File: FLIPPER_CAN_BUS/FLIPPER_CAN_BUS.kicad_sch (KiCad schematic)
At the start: 24 parts, among them J1 Conn_01x02, J1 Conn_01x08_Socket, J2 Conn_01x10_Socket, U1 TJA1051T/3, U2 MCP2515-xST, U3 AP3602AKTR-G1, Y1 16 Mhz

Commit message: Change_Capacitor_BOM
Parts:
- C1, C5: manf# C0603C470J4GACAUTO -> FN18N220J500PSG
- C10, C12, C13, C8: LCSC# (none) -> C326057; Proveedor Mouser -> LCSC; manf# KAM15CT70J106KT -> CC0603KRX5R6BB106
- C11, C2, C7, C9: LCSC# (none) -> C282519; Proveedor Mouser -> LCSC; manf# 0603F104Z160CT -> TCC0603X7R104K500CT
- C3, C4: LCSC# (none) -> C525244; Proveedor Mouser -> LCSC
- C6: LCSC# (none) -> C26413; Proveedor Mouser -> LCSC; manf# 06035C105KAT2A -> CL10A105KP8NNNC
- R1, R3: LCSC# (none) -> C99198; Proveedor Mouser -> LCSC; manf# RP0603DRD0710KL -> RC0603JR-0710KL
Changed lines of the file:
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@@
       (effects (font (size 1.27 1.27)) hide)
     )
-    (property "manf#" "KAM15CT70J106KT" (at 208.153 106.172 0)
-      (effects (font (size 1.27 1.27)) hide)
-    )
-    (property "Proveedor" "Mouser" (at 208.153 106.172 0)
+    (property "manf#" "CC0603KRX5R6BB106" (at 208.153 106.172 0)
+      (effects (font (size 1.27 1.27)) hide)
+    )
+    (property "Proveedor" "LCSC" (at 208.153 106.172 0)
+      (effects (font (size 1.27 1.27)) hide)
+    )
+    (property "LCSC#" "C326057" (at 208.153 106.172 0)
       (effects (font (size 1.27 1.27)) hide)
     )
@@
       (effects (font (size 1.27 1.27)) hide)
     )
-    (property "manf#" "C0603C470J4GACAUTO" (at 205.105 56.134 0)
+    (property "manf#" "FN18N220J500PSG" (at 205.105 56.134 0)
       (effects (font (size 1.27 1.27)) hide)
     )
@@
       (effects (font (size 1.27 1.27)) hide)
     )
-    (property "manf#" "KAM15CT70J106KT" (at 146.558 109.22 0)
-      (effects (font (size 1.27 1.27)) hide)
-    )
-    (property "Proveedor" "Mouser" (at 146.558 109.22 0)
+    (property "manf#" "CC0603KRX5R6BB106" (at 146.558 109.22 0)
+      (effects (font (size 1.27 1.27)) hide)
+    )
+    (property "Proveedor" "LCSC" (at 146.558 109.22 0)
+      (effects (font (size 1.27 1.27)) hide)
+    )
+    (property "LCSC#" "C326057" (at 146.558 109.22 0)
       (effects (font (size 1.27 1.27)) hide)
     )
@@
       (effects (font (size 1.27 1.27)) hide)
     )
-    (property "manf#" "RP0603DRD0710KL" (at 130.81 49.403 0)
-      (effects (font (size 1.27 1.27)) hide)
-    )
-    (property "Proveedor" "Mouser" (at 130.81 49.403 0)
+    (property "manf#" "RC0603JR-0710KL" (at 130.81 49.403 0)
+      (effects (font (size 1.27 1.27)) hide)
+    )
+    (property "Proveedor" "LCSC" (at 130.81 49.403 0)
+      (effects (font (size 1.27 1.27)) hide)
+    )
+    (property "LCSC#" "C99198" (at 130.81 49.403 0)
       (effects (font (size 1.27 1.27)) hide)
     )
@@
       (effects (font (size 1.27 1.27)) hide)
     )
-    (property "manf#" "KAM15CT70J106KT" (at 132.334 100.457 0)
-      (effects (font (size 1.27 1.27)) hide)
-    )
-    (property "Proveedor" "Mouser" (at 132.334 100.457 0)
+    (property "manf#" "CC0603KRX5R6BB106" (at 132.334 100.457 0)
+      (effects (font (size 1.27 1.27)) hide)
+    )
+    (property "Proveedor" "LCSC" (at 132.334 100.457 0)
+      (effects (font (size 1.27 1.27)) hide)
+    )
+    (property "LCSC#" "C326057" (at 132.334 100.457 0)
       (effects (font (size 1.27 1.27)) hide)
     )
@@
       (effects (font (size 1.27 1.27)) hide)
     )
-    (property "manf#" "0603F104Z160CT" (at 124.714 100.457 0)
-      (effects (font (size 1.27 1.27)) hide)
-    )
-    (property "Proveedor" "Mouser" (at 124.714 100.457 0)
+    (property "manf#" "TCC0603X7R104K500CT" (at 124.714 100.457 0)
+      (effects (font (size 1.27 1.27)) hide)
+    )
+    (property "Proveedor" "LCSC" (at 124.714 100.457 0)
+      (effects (font (size 1.27 1.27)) hide)
+    )
+    (property "LCSC#" "C282519" (at 124.714 100.457 0)
       (effects (font (size 1.27 1.27)) hide)
     )
@@
       (effects (font (size 1.27 1.27)) hide)
     )
-    (property "Proveedor" "Mouser" (at 19.685 48.514 0)
+    (property "Proveedor" "LCSC" (at 19.685 48.514 0)
+      (effects (font (size 1.27 1.27)) hide)
+    )
+    (property "LCSC#" "C525244" (at 19.685 48.514 0)
       (effects (font (size 1.27 1.27)) hide)
     )
@@
       (effects (font (size 1.27 1.27)) hide)
     )
-    (property "Proveedor" "Mouser" (at 19.685 56.134 0)
+    (property "Proveedor" "LCSC" (at 19.685 56.134 0)
+      (effects (font (size 1.27 1.27)) hide)
+    )
+    (property "LCSC#" "C525244" (at 19.685 56.134 0)
       (effects (font (size 1.27 1.27)) hide)
     )
@@
       (effects (font (size 1.27 1.27)) hide)
     )
-    (property "manf#" "KAM15CT70J106KT" (at 225.933 100.457 0)
-      (effects (font (size 1.27 1.27)) hide)
-    )
-    (property "Proveedor" "Mouser" (at 225.933 100.457 0)
+    (property "manf#" "CC0603KRX5R6BB106" (at 225.933 100.457 0)
+      (effects (font (size 1.27 1.27)) hide)
+    )
+    (property "Proveedor" "LCSC" (at 225.933 100.457 0)
+      (effects (font (size 1.27 1.27)) hide)
+    )
+    (property "LCSC#" "C326057" (at 225.933 100.457 0)
       (effects (font (size 1.27 1.27)) hide)
     )
@@
       (effects (font (size 1.27 1.27)) hide)
     )
-    (property "manf#" "06035C105KAT2A" (at 155.194 97.282 0)
-      (effects (font (size 1.27 1.27)) hide)
-    )
-    (property "Proveedor" "Mouser" (at 155.194 97.282 0)
+    (property "manf#" "CL10A105KP8NNNC" (at 155.194 97.282 0)
+      (effects (font (size 1.27 1.27)) hide)
+    )
+    (property "Proveedor" "LCSC" (at 155.194 97.282 0)
+      (effects (font (size 1.27 1.27)) hide)
+    )
+    (property "LCSC#" "C26413" (at 155.194 97.282 0)
       (effects (font (size 1.27 1.27)) hide)
     )
@@
       (effects (font (size 1.27 1.27)) hide)
     )
-    (property "manf#" "C0603C470J4GACAUTO" (at 204.724 21.082 0)
+    (property "manf#" "FN18N220J500PSG" (at 204.724 21.082 0)
       (effects (font (size 1.27 1.27)) hide)
     )
@@
       (effects (font (size 1.27 1.27)) hide)
     )
-    (property "manf#" "0603F104Z160CT" (at 58.039 23.368 0)
-      (effects (font (size 1.27 1.27)) hide)
-    )
-    (property "Proveedor" "Mouser" (at 58.039 23.368 0)
+    (property "manf#" "TCC0603X7R104K500CT" (at 58.039 23.368 0)
+      (effects (font (size 1.27 1.27)) hide)
+    )
+    (property "Proveedor" "LCSC" (at 58.039 23.368 0)
+      (effects (font (size 1.27 1.27)) hide)
+    )
+    (property "LCSC#" "C282519" (at 58.039 23.368 0)
       (effects (font (size 1.27 1.27)) hide)
     )
@@
       (effects (font (size 1.27 1.27)) hide)
     )
-    (property "manf#" "RP0603DRD0710KL" (at 35.687 29.845 0)
-      (effects (font (size 1.27 1.27)) hide)
-    )
-    (property "Proveedor" "Mouser" (at 35.687 29.845 0)
+    (property "manf#" "RC0603JR-0710KL" (at 35.687 29.845 0)
+      (effects (font (size 1.27 1.27)) hide)
+    )
+    (property "Proveedor" "LCSC" (at 35.687 29.845 0)
+      (effects (font (size 1.27 1.27)) hide)
+    )
+    (property "LCSC#" "C99198" (at 35.687 29.845 0)
       (effects (font (size 1.27 1.27)) hide)
     )
@@
       (effects (font (size 1.27 1.27)) hide)
     )
-    (property "manf#" "0603F104Z160CT" (at 218.313 100.457 0)
-      (effects (font (size 1.27 1.27)) hide)
-    )
-    (property "Proveedor" "Mouser" (at 218.313 100.457 0)
+    (property "manf#" "TCC0603X7R104K500CT" (at 218.313 100.457 0)
+      (effects (font (size 1.27 1.27)) hide)
+    )
+    (property "Proveedor" "LCSC" (at 218.313 100.457 0)
+      (effects (font (size 1.27 1.27)) hide)
+    )
+    (property "LCSC#" "C282519" (at 218.313 100.457 0)
       (effects (font (size 1.27 1.27)) hide)
     )
@@
       (effects (font (size 1.27 1.27)) hide)
     )
-    (property "manf#" "0603F104Z160CT" (at 240.284 100.584 0)
-      (effects (font (size 1.27 1.27)) hide)
-    )
-    (property "Proveedor" "Mouser" (at 240.284 100.584 0)
-      (effects (font (size 1.27 1.27)) hide)
-    )
+    (property "manf#" "TCC0603X7R104K500CT" (at 240.284 100.584 0)
+      (effects (font (size 1.27 1.27)) hide)
+    )
+    (property "Proveedor" "LCSC" (at 240.284 100.584 0)
+      (effects (font (size 1.27 1.27)) hide)
+    )
+    (property "LCSC#" "C282519" (at 240.284 100.584 0)
+      (effects (font (size 1.27 1.27)) hide)
+    )

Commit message: Update BOM flipper_can_bus
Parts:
- D1: LCSC# (none) -> C907839; Proveedor Mouser -> LCSC
- J1: LCSC# (none) -> C2894950; Proveedor Mouser -> LCSC; manf# M20-9961045 -> PZ254-1-08-W-8.5
- J2: LCSC# (none) -> C492418; Proveedor Mouser -> LCSC; manf# M20-9961045 -> PZ254R-11-10P
- U1: LCSC# (none) -> C58988
- U2: manf# (none) -> MCP2515-I/ST
- U3: LCSC# (none) -> C460358
- Y1: manf# (none) -> X2C016000B91H-R
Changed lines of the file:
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@@
       (effects (font (size 1.27 1.27)) hide)
     )
-    (property "manf#" "" (at 29.845 52.324 90)
+    (property "manf#" "X2C016000B91H-R" (at 29.845 52.324 90)
       (effects (font (size 1.27 1.27)) hide)
     )
@@
     )
     (property "Proveedor" "Mouser" (at 201.295 101.219 0)
+      (effects (font (size 1.27 1.27)) hide)
+    )
+    (property "LCSC#" "C460358" (at 201.295 101.219 0)
       (effects (font (size 1.27 1.27)) hide)
     )
@@
       (effects (font (size 1.27 1.27)) hide)
     )
-    (property "Proveedor" "Mouser" (at 80.645 103.886 0)
-      (effects (font (size 1.27 1.27)) hide)
-    )
-    (property "manf#" "M20-9961045" (at 80.645 103.886 0)
+    (property "Proveedor" "LCSC" (at 80.645 103.886 0)
+      (effects (font (size 1.27 1.27)) hide)
+    )
+    (property "manf#" "PZ254-1-08-W-8.5" (at 80.645 103.886 0)
+      (effects (font (size 1.27 1.27)) hide)
+    )
+    (property "LCSC#" "C2894950" (at 80.645 103.886 0)
       (effects (font (size 1.27 1.27)) hide)
     )
@@
       (effects (font (size 1.27 1.27)) hide)
     )
-    (property "LCSC#" "" (at 50.165 101.473 0)
-      (effects (font (size 1.27 1.27)) hide)
-    )
-    (property "Proveedor" "Mouser" (at 50.165 101.473 0)
-      (effects (font (size 1.27 1.27)) hide)
-    )
-    (property "manf#" "M20-9961045" (at 50.165 101.473 0)
+    (property "LCSC#" "C492418" (at 50.165 101.473 0)
+      (effects (font (size 1.27 1.27)) hide)
+    )
+    (property "Proveedor" "LCSC" (at 50.165 101.473 0)
+      (effects (font (size 1.27 1.27)) hide)
+    )
+    (property "manf#" "PZ254R-11-10P" (at 50.165 101.473 0)
       (effects (font (size 1.27 1.27)) hide)
     )
@@
       (effects (font (size 1.27 1.27)) hide)
     )
-    (property "Proveedor" "Mouser" (at 235.839 33.528 0)
+    (property "Proveedor" "LCSC" (at 235.839 33.528 0)
+      (effects (font (size 1.27 1.27)) hide)
+    )
+    (property "LCSC#" "C907839" (at 235.839 33.528 0)
       (effects (font (size 1.27 1.27)) hide)
     )
@@
       (effects (font (size 1.27 1.27)) hide)
     )
-    (property "manf#" "" (at 64.135 46.228 0)
+    (property "manf#" "MCP2515-I/ST" (at 64.135 46.228 0)
       (effects (font (size 1.27 1.27)) hide)
     )
@@
       (effects (font (size 1.27 1.27)) hide)
     )
+    (property "LCSC#" "C58988" (at 152.527 41.148 0)
+      (effects (font (size 1.27 1.27)) hide)
+    )

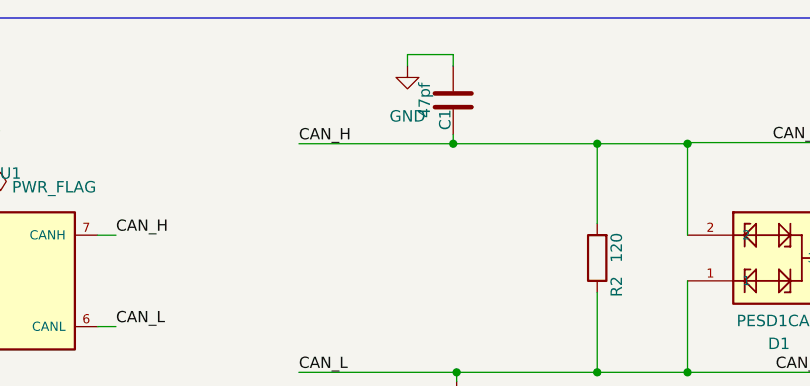
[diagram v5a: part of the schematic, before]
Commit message: Fix C1 part Flippper_can_bus
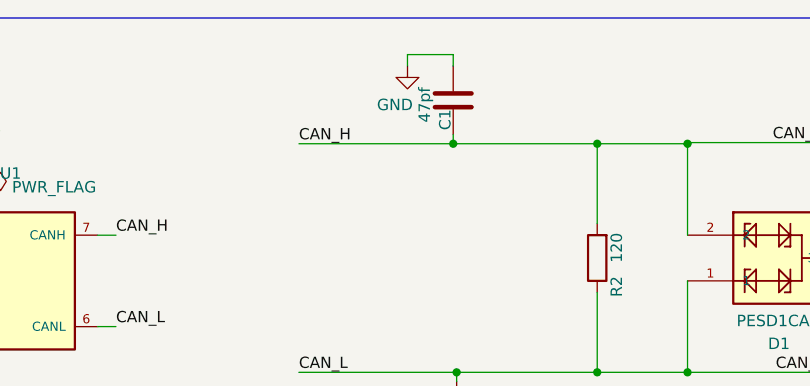
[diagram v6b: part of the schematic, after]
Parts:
- C1, C5: LCSC# (none) -> C105622; Proveedor Mouser -> LCSC; manf# FN18N220J500PSG -> CC0603JRNPO9BN470
- R2: LCSC# (none) -> C365072; Proveedor Mouser -> LCSC; manf# CRGH0603J120R -> HPCR0603F120RK9
- U1, U3: Proveedor Mouser -> LCSC
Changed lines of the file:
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@@
       (effects (font (size 1.27 1.27)) hide)
     )
-    (property "manf#" "FN18N220J500PSG" (at 205.105 56.134 0)
-      (effects (font (size 1.27 1.27)) hide)
-    )
-    (property "Proveedor" "Mouser" (at 205.105 56.134 0)
+    (property "manf#" "CC0603JRNPO9BN470" (at 205.105 56.134 0)
+      (effects (font (size 1.27 1.27)) hide)
+    )
+    (property "Proveedor" "LCSC" (at 205.105 56.134 0)
+      (effects (font (size 1.27 1.27)) hide)
+    )
+    (property "LCSC#" "C105622" (at 205.105 56.134 0)
       (effects (font (size 1.27 1.27)) hide)
     )
@@
       (effects (font (size 1.27 1.27)) hide)
     )
-    (property "manf#" "CRGH0603J120R" (at 220.726 38.608 0)
-      (effects (font (size 1.27 1.27)) hide)
-    )
-    (property "Proveedor" "Mouser" (at 220.726 38.608 0)
+    (property "manf#" "HPCR0603F120RK9" (at 220.726 38.608 0)
+      (effects (font (size 1.27 1.27)) hide)
+    )
+    (property "Proveedor" "LCSC" (at 220.726 38.608 0)
+      (effects (font (size 1.27 1.27)) hide)
+    )
+    (property "LCSC#" "C365072" (at 220.726 38.608 0)
       (effects (font (size 1.27 1.27)) hide)
     )
@@
       (effects (font (size 1.27 1.27)) hide)
     )
-    (property "Proveedor" "Mouser" (at 201.295 101.219 0)
+    (property "Proveedor" "LCSC" (at 201.295 101.219 0)
       (effects (font (size 1.27 1.27)) hide)
     )
@@
       (effects (font (size 1.27 1.27)))
     )
-    (property "Value" "47pf" (at 201.549 21.082 90)
+    (property "Value" "47pf" (at 201.549 21.59 90)
       (effects (font (size 1.27 1.27)))
     )
@@
       (effects (font (size 1.27 1.27)) hide)
     )
-    (property "manf#" "FN18N220J500PSG" (at 204.724 21.082 0)
-      (effects (font (size 1.27 1.27)) hide)
-    )
-    (property "Proveedor" "Mouser" (at 204.724 21.082 0)
+    (property "manf#" "CC0603JRNPO9BN470" (at 204.724 21.082 0)
+      (effects (font (size 1.27 1.27)) hide)
+    )
+    (property "Proveedor" "LCSC" (at 204.724 21.082 0)
+      (effects (font (size 1.27 1.27)) hide)
+    )
+    (property "LCSC#" "C105622" (at 204.724 21.082 0)
       (effects (font (size 1.27 1.27)) hide)
     )
@@
   )
   (symbol (lib_id "power:GND") (at 199.644 17.272 0) (unit 1)
-    (in_bom yes) (on_board yes) (dnp no) (fields_autoplaced)
+    (in_bom yes) (on_board yes) (dnp no)
     (property "Reference" "#PWR01" (at 199.644 23.622 0)
       (effects (font (size 1.27 1.27)) hide)
     )
-    (property "Value" "GND" (at 199.644 22.86 0)
+    (property "Value" "GND" (at 198.247 21.59 0)
       (effects (font (size 1.27 1.27)))
     )
@@
       (effects (font (size 1.27 1.27)) hide)
     )
-    (property "Proveedor" "Mouser" (at 152.527 41.148 0)
-      (effects (font (size 1.27 1.27)) hide)
-    )
+    (property "Proveedor" "LCSC" (at 152.527 41.148 0)
+      (effects (font (size 1.27 1.27)) hide)
+    )
